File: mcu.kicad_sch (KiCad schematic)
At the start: 9 parts, among them IC1 TMP235A4DCKR, U1 STM32H563RGTx

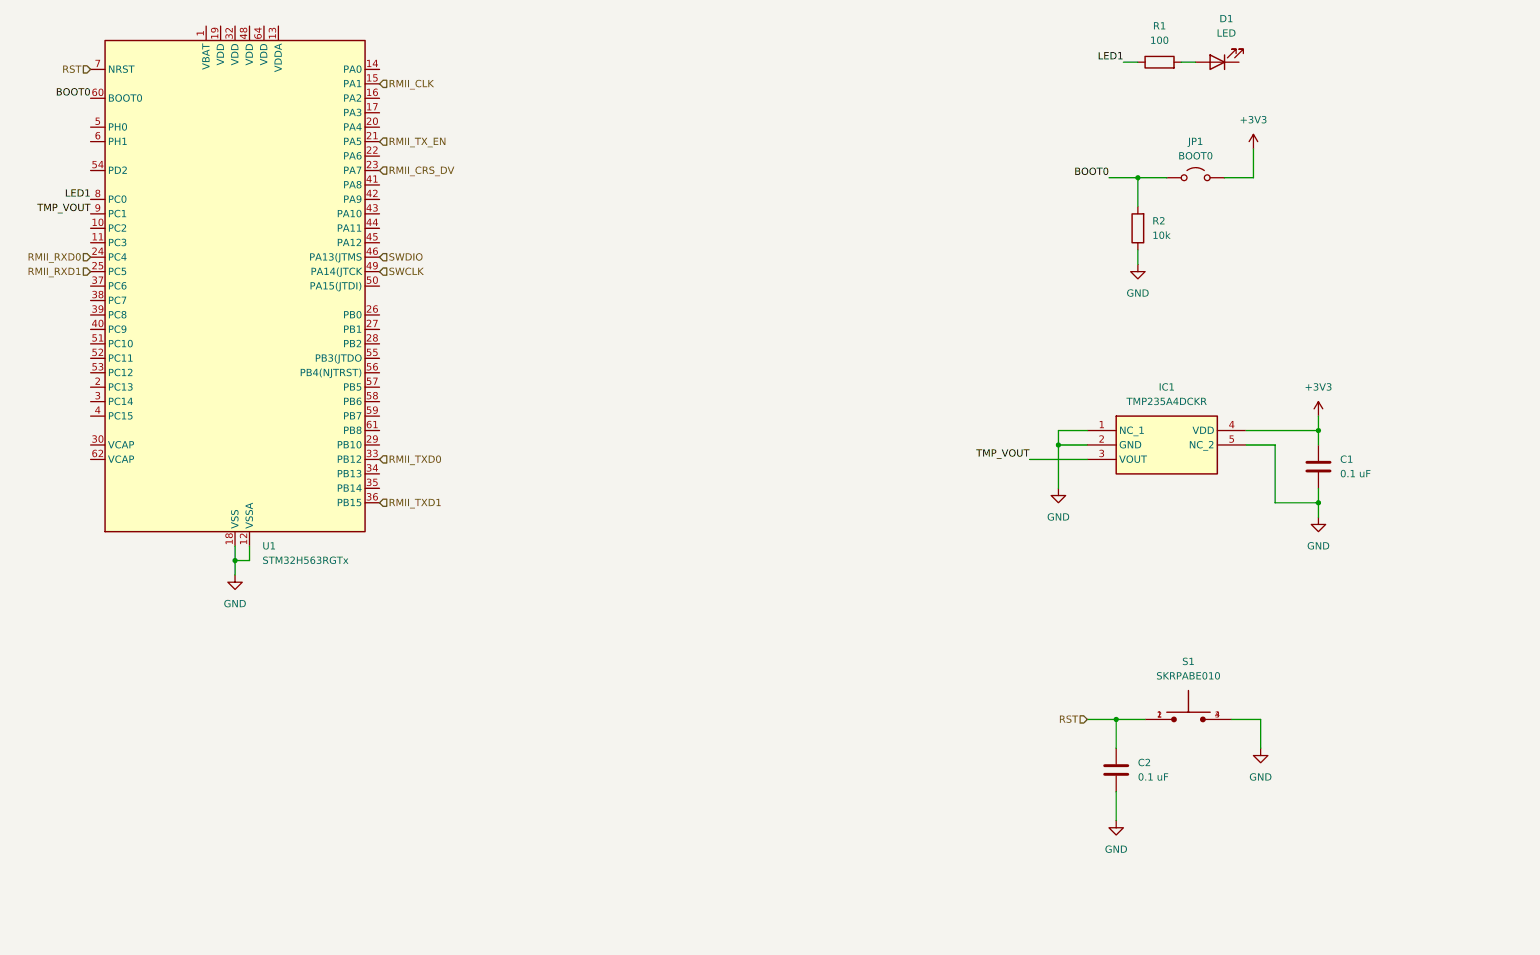
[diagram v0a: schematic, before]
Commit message: Add power sheet and update schematic connections
Added a new power sheet to the project and updated the main schematic to include connections for power, MCU, peripherals, and Ethernet PHY. Also added backup files and updated the Ethernet PHY schematic with symbol definitions and pin mappings.
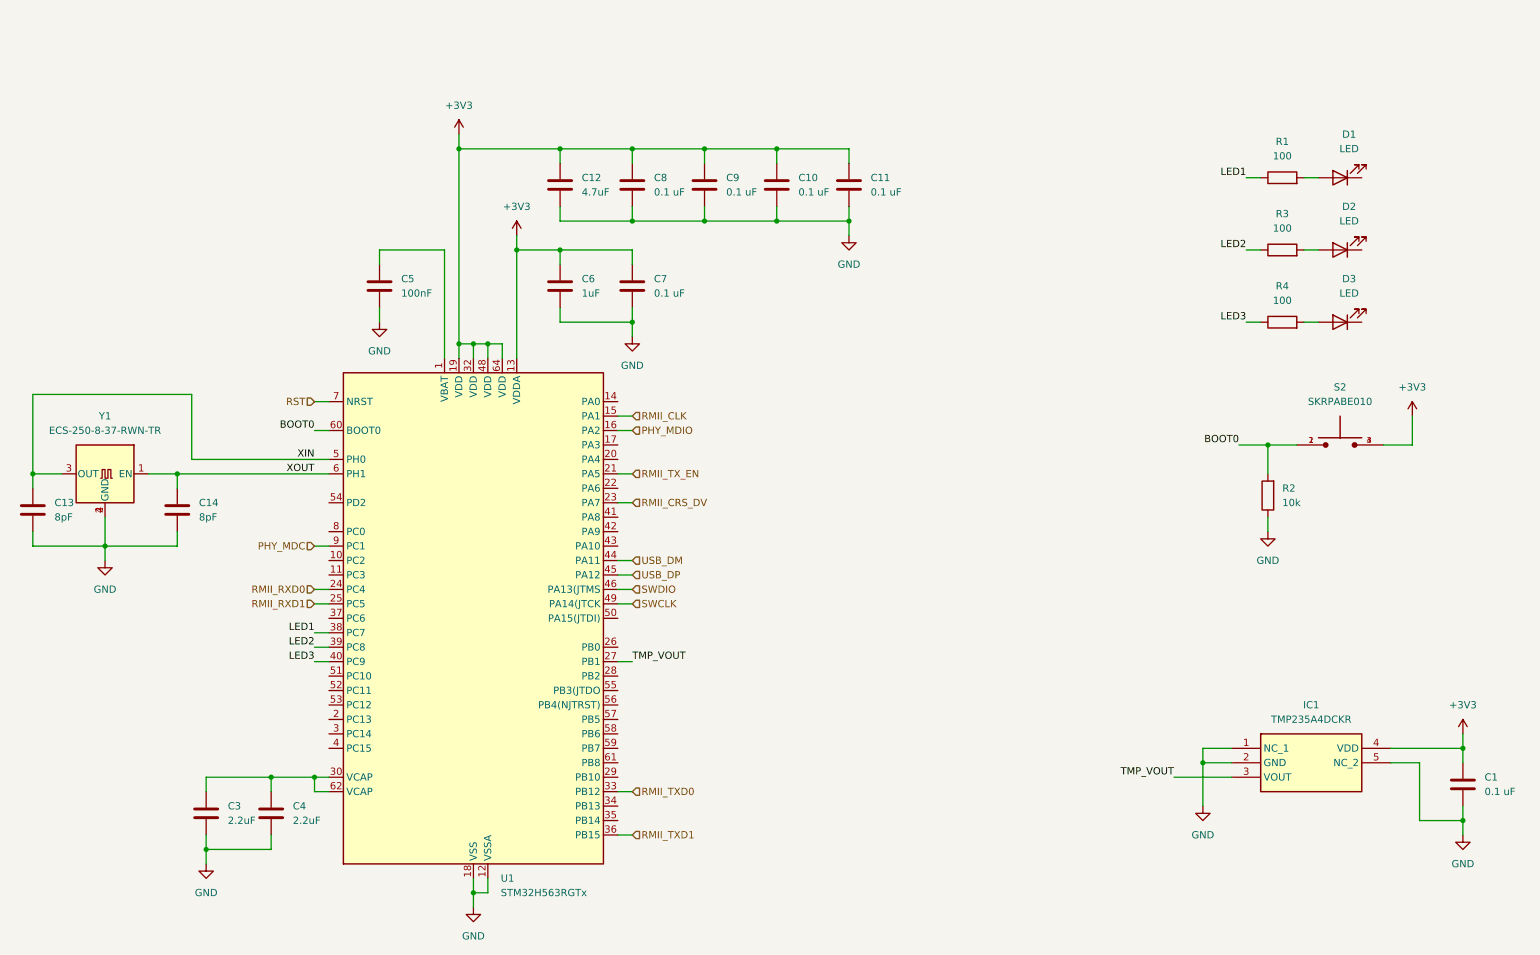
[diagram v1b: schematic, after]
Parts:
- removed C2: 0.1 uF, symbol Device:C
- removed JP1: BOOT0, symbol Jumper:Jumper_2_Open
- removed S1: SKRPABE010, SKRPABE010:SW_SKRPABE010, symbol SKRPABE010:SKRPABE010
- added C10, C11, C7, C8, C9: 0.1 uF, symbol Device:C
- added C12: 4.7uF, symbol Device:C
- added C13, C14: 8pF, symbol Device:C
- added C3, C4: 2.2uF, symbol Device:C
- added C5: 100nF, symbol Device:C
- added C6: 1uF, symbol Device:C
- added D2, D3: LED, symbol Device:LED
- added R3, R4: 100, symbol Device:R
- added S2: SKRPABE010, SKRPABE010:SW_SKRPABE010, symbol SKRPABE010:SKRPABE010
- added Y1: ECS-250-8-37-RWN-TR, Crystal:Crystal_SMD_SeikoEpson_FA128-4Pin_2.0x1.6mm, symbol MyLibrary:ECS-250-8-37-RWN-TR
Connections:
- net +3V3: now also U1.13 (VDDA), U1.19 (VDD), U1.32 (VDD), U1.48 (VDD), U1.64 (VDD), C10.1, C11.1, C12.2, C6.1, C7.1, C8.1, C9.1, S2.3, S2.4
- net BOOT0: now also S2.1, S2.2
- net GND: now also C10.2, C11.2, C12.1, C13.2, C14.2, C3.2, C4.2, C5.1, C6.2, C7.2, C8.2, C9.2, Y1.2 (GND), Y1.4 (GND)
- net LED1: now also U1.38 (PC7); no longer U1.8 (PC0)
- net TMP_VOUT: now also U1.27 (PB1); no longer U1.9 (PC1)
- net at U1.1 (VBAT): now also C5.2
- net PHY_MDIO: now reaches U1.16 (PA2)
- net at U1.30 (VCAP): now also U1.62 (VCAP), C3.1, C4.1
- net LED2: now reaches U1.39 (PC8)
- net LED2: now also R3.1
- net LED3: now reaches U1.40 (PC9)
- net LED3: now also R4.1
- net USB_DM: now reaches U1.44 (PA11)
- net USB_DP: now reaches U1.45 (PA12)
- net XIN: now reaches U1.5 (PH0)
- net XIN: now also C13.1, Y1.3 (OUT)
- net XOUT: now reaches U1.6 (PH1)
- net XOUT: now also C14.1, Y1.1 (EN)
- new net: D3.2 (A), R4.2
- new net: D2.2 (A), R3.2
- new net PHY_MDC: U1.9 (PC1)
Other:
- moved on the sheet: C1, D1, IC1, R1, R2, U1

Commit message: Update schematic power symbols and add backups
Replaced +48V and -48V power symbols with VDD and VSS in peripherals.kicad_sch, updated title blocks and paper sizes in all .kicad_sch files, and added new schematic symbols for test points, capacitors, resistors, MOSFET, and optocoupler in power.kicad_sch. Added multiple new backup ZIP files for POETempSensor.
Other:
- title: (none) -> MCU
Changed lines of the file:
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@@
 	(generator_version "9.0")
 	(paper "A3")
+	(title_block
+		(title "MCU")
+		(date "2025-11-09")
+		(rev "v0.1")
+	)
